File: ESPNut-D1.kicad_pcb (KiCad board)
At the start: 2 copper layers, 44 x 20 mm, 87 parts, among them J1 USB_C_Receptacle_USB2.0, J2 ESP_CONN, J3 ESP_CONN, J4 USB_PADS, J5 ESP_PROG, Q1 BC817, Q2 BC817, SW1 ESP_RST, SW2 ESP_BOOT, SW3 ESP_VDD_SW, SW4 ESPV_SEL, SW5 POW_CTRL, U1 CH340G, U2 MIC5219-3.3YM5, U3 AP22804AW5, Y1 12MHz

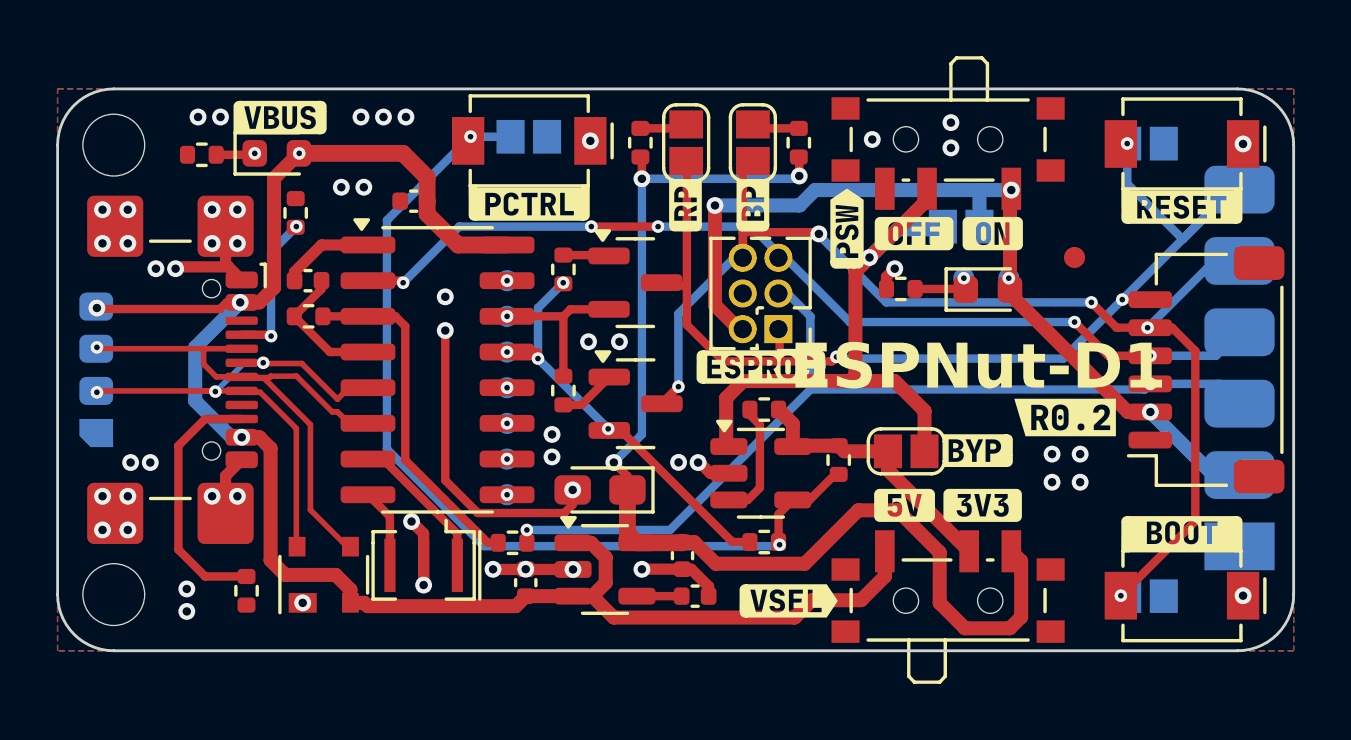
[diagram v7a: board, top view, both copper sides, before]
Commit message: New Revision `R0.3` - Schematic   - Added DPDT `UART_SWAP` switch to swap the `TX` and `RX` lines.     - But this is DNPed because the switch consumes too much space.   - Added UART activity LEDs on both `TX` and `RX` lines.   - Changed all existing transistor footprints to `SOT-523`.   - Excluded `AP22804AW5`'s `FLG` resistor from the board.   - Updated the BoM.   - Reset the annotations. - PCB   - Imported all changes to the PCB.   - Updated placements.   - Routing completed.   - Updated Fab layers.   - DRC passes. - Generated manufacturing files. - Schematic   - Added `DIFF` class for differential pairs.   - Added `1K` series resistors to both the `TX` and `RX` lines.     - This will limit the current and reverse voltage to the target.     - Previously we only had a single `220R` resistor on the `RX` line of the `CH340`.     - A value of `1K` does not affect performance. - New Revision 🆕 `R0.3`.
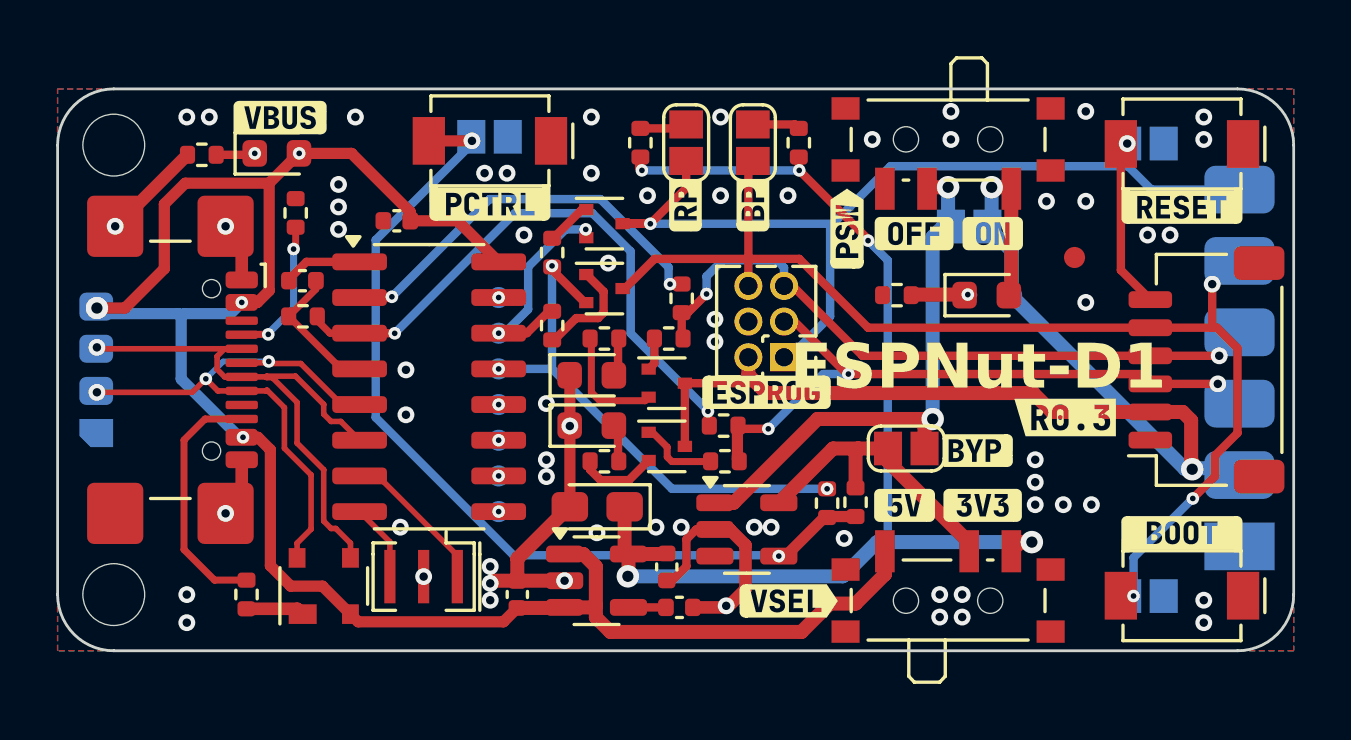
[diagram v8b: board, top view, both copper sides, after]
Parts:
- removed the R12 at (144.2, 81.4)
- removed kibuzzard-688268E7: G***, kibuzzard-688268E7
- removed kibuzzard-6883846F: G***, kibuzzard-6883846F
- added D4: RX_LED, LED_SMD:LED_0603_1608Metric, F.Cu at (138.0, 80.2)
- added D5: TX_LED, LED_SMD:LED_0603_1608Metric, F.Cu at (138.0, 82.0)
- added Q3: MMBT3906T-7-F, CSE_Package_TO_SOT_SMD:SOT-523, F.Cu at (140.7, 80.5)
- added Q4: MMBT3906T-7-F, CSE_Package_TO_SOT_SMD:SOT-523, F.Cu at (140.7, 82.7)
- added R15: 1K, Resistor_SMD:R_0402_1005Metric, F.Cu at (140.8, 78.9)
- added R16: 1K, Resistor_SMD:R_0402_1005Metric, F.Cu at (142.8, 83.3)
- added R17: 220R, Resistor_SMD:R_0402_1005Metric, F.Cu at (138.5, 78.9)
- added R18: 220R, Resistor_SMD:R_0402_1005Metric, F.Cu at (138.5, 83.3)
- added R6: 1K, Resistor_SMD:R_0402_1005Metric, F.Cu at (141.2, 77.5)
- added kibuzzard-688DAF86: G***, kibuzzard-688DAF86, F.Cu at (154.9, 81.7)
- added kibuzzard-688DAF8E: G***, kibuzzard-688DAF8E, B.Cu at (138.4, 77.2)
- Q1, Q2: value BC817 -> MMBT3904T-7-F; footprint Package_TO_SOT_SMD:SOT-23 -> CSE_Package_TO_SOT_SMD:SOT-523
- R8: renamed from R7; value 220R -> 1K
- moved R8 8.59 mm to (142.7, 82.0)
- moved Q2 4.25 mm to (138.5, 77.1)
- moved G*** 2.80 mm to (128.2, 84.6)
- moved R12 2.63 mm to (146.4, 84.7), turned to 90 degrees
- moved Q1 2.37 mm to (138.5, 74.8)
- moved R10 2.35 mm to (136.6, 78.4)
- moved G*** 2.32 mm to (146.8, 83.2)
- moved U3 2.06 mm to (143.5, 85.7)
- moved R11 1.62 mm to (147.4, 84.7)
- moved JP7 1.40 mm to (134.4, 71.7)
- moved SW5 1.40 mm to (134.4, 71.8)
- moved kibuzzard-67F0C2BD 1.40 mm to (131.3, 71.7)
- moved kibuzzard-68827490 1.40 mm to (134.4, 74.1)
- moved J5 1.02 mm to (144.9, 79.6)
- moved C2 0.92 mm to (131.1, 74.7)
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- renumbered J4 to J2, J2 to J3, J3 to J4, R9 to R10, R10 to R11, R11 to R12, R13 to R14, R6 to R7, R8 to R9
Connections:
- net /ESP_TX0 renamed /CH_RX
- J3 pad 4: /ESP_RX0 -> /CH_TX
- J4 pad 4: /ESP_RX0 -> /CH_TX
- J5 pad 5: /ESP_RX0 -> /CH_TX
- U1 pad 2: /ESP_RX0 -> Net-(U1-TXD)
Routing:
- net /ESP_RX0: track 34.2 -> 0.00 mm, vias 5 -> 0
- net /CH_TX: track 0.00 -> 23.0 mm, vias 0 -> 2
- net Net-(U1-TXD): track 0.00 -> 14.5 mm, vias 0 -> 2
- net /ESP_VDD_O: track 31.6 -> 43.5 mm, vias 4 -> 2
- net /CH_RX: track 32.3 -> 22.5 mm, vias 2 -> 3
- net Net-(U1-RXD): track 12.4 -> 21.2 mm, vias 0 -> 2
- net VBUS: track 60.6 -> 68.7 mm
- net /DTR: track 14.6 -> 18.9 mm, vias 4 -> 3
- net Net-(U3-~{FLG}): track 4.21 -> 0.00 mm
- net Net-(Q3-E): track 0.00 -> 4.17 mm
- net Net-(JP5-A): track 22.5 -> 19.7 mm, vias 1 -> 2
- net Net-(Q4-B): track 0.00 -> 2.84 mm
- net Net-(Q4-E): track 0.00 -> 2.83 mm
- net /RTS: track 5.86 -> 8.05 mm, vias 1 -> 2
- net Net-(Q2-B): track 2.04 -> 3.84 mm
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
